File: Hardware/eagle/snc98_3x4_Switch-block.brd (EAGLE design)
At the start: 56.4 x 83.2 mm, 67 parts

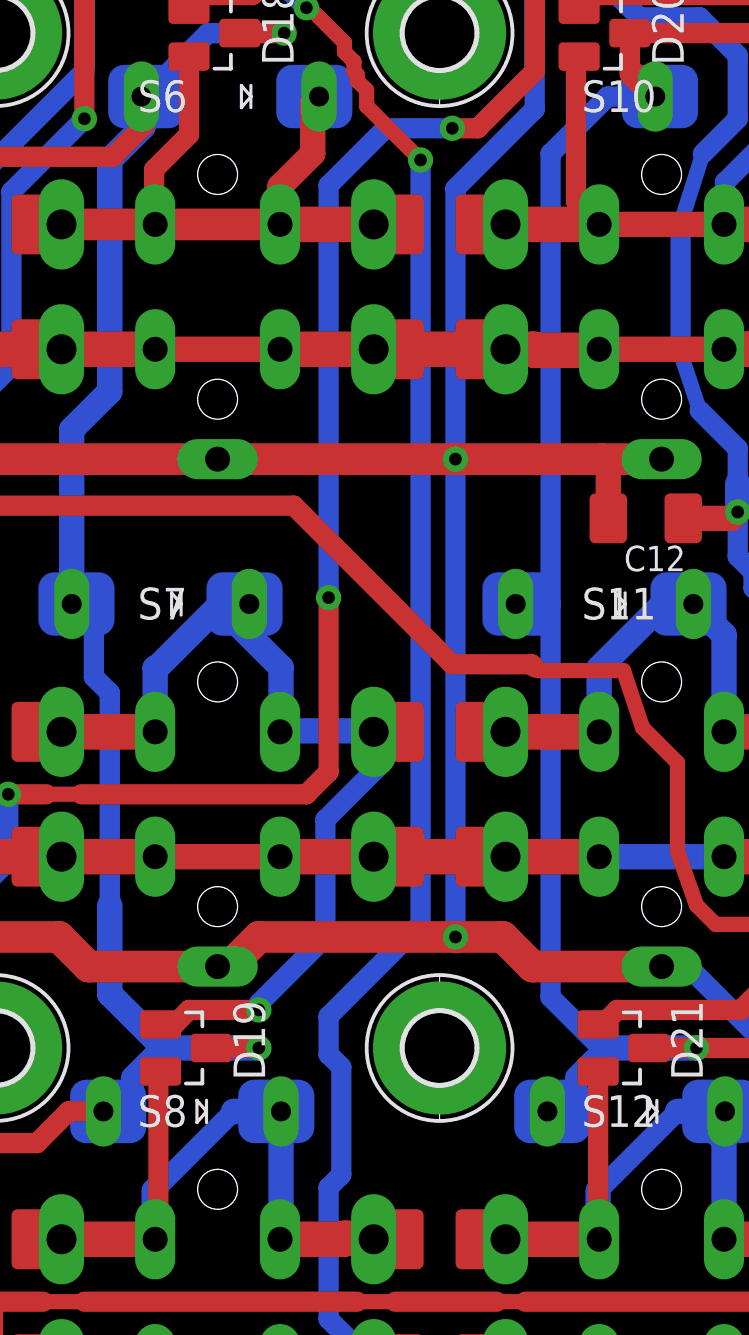
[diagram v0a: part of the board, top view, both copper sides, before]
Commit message: MR(); MS(); M+=(); Display Status
Display whe to or more switch pressed.
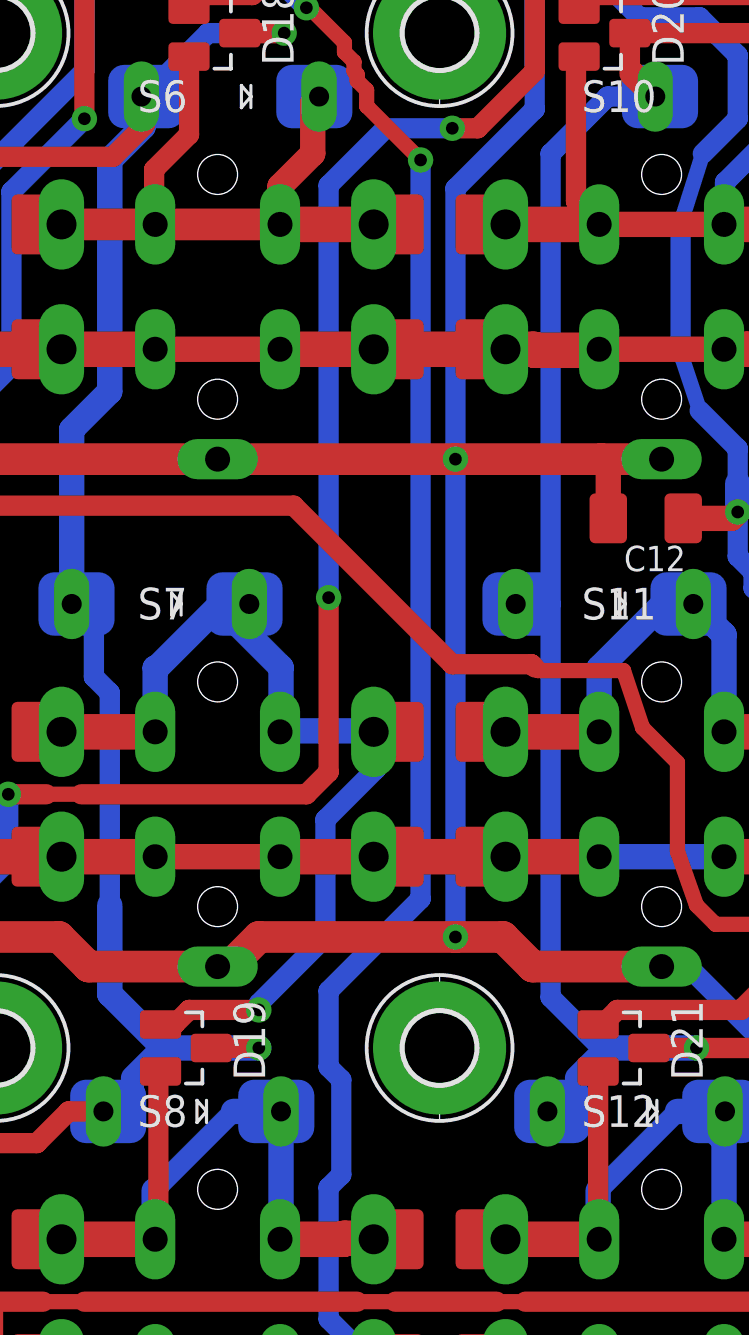
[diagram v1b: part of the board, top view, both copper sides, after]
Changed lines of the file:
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@@
 <setting verticaltext="up"/>
 </settings>
-<grid distance="5" unitdist="mil" unit="mil" style="lines" multiple="1" display="yes" altdistance="0.01" altunitdist="inch" altunit="inch"/>
+<grid distance="0.1" unitdist="inch" unit="inch" style="lines" multiple="1" display="yes" altdistance="0.01" altunitdist="inch" altunit="inch"/>
 <layers>
 <layer number="1" name="Top" color="4" fill="1" visible="yes" active="yes"/>
@@
 <via x="31.75" y="62.865" extent="1-16" drill="0.508"/>
 <via x="36.322" y="56.769" extent="1-16" drill="0.508"/>
-<wire x1="36.322" y1="56.769" x2="36.322" y2="26.162" width="0.8128" layer="16"/>
+<wire x1="36.322" y1="56.769" x2="36.322" y2="27.178" width="0.8128" layer="16"/>
 <wire x1="32.639" y1="10.354" x2="34.444" y2="8.549" width="0.8128" layer="16"/>
 <wire x1="30.861" y1="66.294" x2="32.639" y2="68.072" width="0.8128" layer="16"/>
@@
 <wire x1="31.877" y1="62.865" x2="33.274" y2="61.468" width="0.6096" layer="1"/>
 <wire x1="30.734" y1="63.881" x2="31.75" y2="62.865" width="0.8128" layer="16"/>
-<wire x1="32.639" y1="20.955" x2="32.639" y2="22.479" width="0.8128" layer="16"/>
-<wire x1="36.322" y1="26.162" x2="32.639" y2="22.479" width="0.8128" layer="16"/>
-<wire x1="32.639" y1="20.955" x2="33.147" y2="20.447" width="0.8128" layer="16"/>
-<wire x1="33.147" y1="20.447" x2="33.147" y2="16.129" width="0.8128" layer="16"/>
+<wire x1="32.639" y1="20.447" x2="32.639" y2="23.495" width="0.8128" layer="16"/>
+<wire x1="36.322" y1="27.178" x2="32.639" y2="23.495" width="0.8128" layer="16"/>
+<wire x1="32.639" y1="20.447" x2="33.147" y2="19.939" width="0.8128" layer="16"/>
+<wire x1="33.147" y1="19.939" x2="33.147" y2="16.129" width="0.8128" layer="16"/>
 <wire x1="33.147" y1="16.129" x2="32.639" y2="15.621" width="0.8128" layer="16"/>
 <wire x1="32.639" y1="15.621" x2="32.639" y2="10.354" width="0.8128" layer="16"/>

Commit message: New Hardware Design V0.4
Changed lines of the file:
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@@
 <setting verticaltext="up"/>
 </settings>
-<grid distance="0.1" unitdist="inch" unit="inch" style="lines" multiple="1" display="yes" altdistance="0.01" altunitdist="inch" altunit="inch"/>
+<grid distance="5" unitdist="mil" unit="mil" style="lines" multiple="1" display="yes" altdistance="0.01" altunitdist="inch" altunit="inch"/>
 <layers>
 <layer number="1" name="Top" color="4" fill="1" visible="yes" active="yes"/>
@@
 <layer number="24" name="bOrigins" color="15" fill="1" visible="yes" active="yes"/>
 <layer number="25" name="tNames" color="7" fill="1" visible="yes" active="yes"/>
-<layer number="26" name="bNames" color="7" fill="1" visible="yes" active="yes"/>
+<layer number="26" name="bNames" color="7" fill="1" visible="no" active="yes"/>
 <layer number="27" name="tValues" color="7" fill="1" visible="no" active="yes"/>
 <layer number="28" name="bValues" color="7" fill="1" visible="no" active="yes"/>
@@
 <wire x1="47.625" y1="57.023" x2="46.736" y2="54.229" width="0.6096" layer="16"/>
 <wire x1="46.736" y1="54.229" x2="46.736" y2="49.022" width="0.8128" layer="16"/>
-<wire x1="46.736" y1="49.022" x2="47.498" y2="46.736" width="0.6096" layer="16"/>
-<wire x1="47.498" y1="46.736" x2="49.022" y2="45.212" width="0.8128" layer="16"/>
-<wire x1="49.022" y1="45.212" x2="49.022" y2="43.815" width="0.8128" layer="16"/>
+<wire x1="46.736" y1="49.022" x2="47.625" y2="46.736" width="0.6096" layer="16"/>
+<wire x1="49.022" y1="45.339" x2="49.022" y2="43.815" width="0.8128" layer="16"/>
 <wire x1="49.022" y1="42.672" x2="49.022" y2="40.894" width="0.8128" layer="16"/>
 <wire x1="49.022" y1="40.894" x2="49.657" y2="40.259" width="0.8128" layer="16"/>
@@
 <wire x1="51.308" y1="37.973" x2="52.578" y2="37.973" width="0.8128" layer="16"/>
 <wire x1="52.578" y1="37.973" x2="54.991" y2="35.56" width="0.8128" layer="16"/>
+<wire x1="47.625" y1="46.736" x2="49.022" y2="45.339" width="0.8128" layer="16"/>
 </signal>
 <signal name="N$21">
@@
 <wire x1="16.256" y1="64.516" x2="13.589" y2="67.183" width="0.6096" layer="16"/>
 <wire x1="13.589" y1="67.183" x2="12.065" y2="67.183" width="0.6096" layer="16"/>
-<wire x1="12.065" y1="67.183" x2="11.811" y2="67.437" width="0.6096" layer="16"/>
+<wire x1="12.065" y1="67.183" x2="11.938" y2="67.31" width="0.6096" layer="16"/>
 <via x="11.176" y="81.661" extent="1-16" drill="0.508"/>
 <wire x1="11.811" y1="82.423" x2="12.065" y2="82.677" width="0.6096" layer="1"/>
@@
 <wire x1="46.609" y1="29.083" x2="46.609" y2="32.639" width="0.6096" layer="1"/>
 <wire x1="46.609" y1="32.639" x2="45.212" y2="34.036" width="0.6096" layer="1"/>
-<wire x1="45.212" y1="34.036" x2="44.45" y2="36.322" width="0.6096" layer="1"/>
-<wire x1="44.45" y1="36.322" x2="41.021" y2="36.322" width="0.6096" layer="1"/>
+<wire x1="45.212" y1="34.036" x2="44.323" y2="36.322" width="0.6096" layer="1"/>
+<wire x1="44.323" y1="36.322" x2="41.021" y2="36.322" width="0.6096" layer="1"/>
 <wire x1="41.021" y1="36.322" x2="40.894" y2="36.449" width="0.6096" layer="1"/>
 <wire x1="40.894" y1="36.449" x2="40.767" y2="36.576" width="0.8128" layer="1"/>
@@
 <via x="15.494" y="42.926" extent="1-16" drill="0.508"/>
 <wire x1="15.494" y1="42.926" x2="31.242" y2="42.926" width="0.8128" layer="1"/>
-<wire x1="11.811" y1="67.437" x2="11.176" y2="69.29820625" width="0.6096" layer="16"/>
+<wire x1="11.938" y1="67.31" x2="11.176" y2="69.29820625" width="0.6096" layer="16"/>
 <wire x1="11.811" y1="82.423" x2="11.811" y2="82.296" width="0.8128" layer="1"/>
 <wire x1="11.811" y1="82.296" x2="11.176" y2="81.661" width="0.8128" layer="1"/>
@@
 <wire x1="8.6995" y1="77.1525" x2="8.636" y2="77.089" width="0.8128" layer="1"/>
 <via x="8.636" y="77.089" extent="1-16" drill="0.508"/>
-<wire x1="7.747" y1="66.167" x2="7.747" y2="64.643" width="0.8128" layer="16"/>
+<wire x1="7.747" y1="66.294" x2="7.747" y2="64.643" width="0.8128" layer="16"/>
 <wire x1="7.747" y1="64.643" x2="9.017" y2="63.373" width="0.8128" layer="16"/>
 <wire x1="9.017" y1="63.373" x2="12.192" y2="63.373" width="0.8128" layer="16"/>
 <wire x1="23.8125" y1="18.669" x2="23.622" y2="18.669" width="0.8128" layer="16"/>
 <wire x1="22.5425" y1="38.989" x2="22.352" y2="38.989" width="0.8128" layer="16"/>
-<wire x1="8.4455" y1="79.629" x2="8.4455" y2="77.4065" width="0.8128" layer="1"/>
+<wire x1="8.4455" y1="79.629" x2="8.4455" y2="77.2795" width="0.8128" layer="1"/>
 <wire x1="8.636" y1="77.089" x2="8.636" y2="76.8985" width="0.6096" layer="16"/>
 <wire x1="8.636" y1="76.8985" x2="9.779" y2="74.93" width="0.6096" layer="16"/>
 <wire x1="9.779" y1="74.93" x2="9.779" y2="68.961" width="0.8128" layer="16"/>
-<wire x1="8.509" y1="66.929" x2="7.747" y2="66.167" width="0.8128" layer="16"/>
-<wire x1="8.509" y1="66.929" x2="9.779" y2="68.961" width="0.6096" layer="16"/>
-<wire x1="8.4455" y1="77.4065" x2="8.636" y2="77.089" width="0.8128" layer="1"/>
+<wire x1="8.382" y1="66.929" x2="9.779" y2="68.961" width="0.6096" layer="16"/>
 <wire x1="24.8285" y1="20.0025" x2="24.8285" y2="19.685" width="0.8128" layer="16"/>
 <wire x1="24.8285" y1="19.685" x2="23.8125" y2="18.669" width="0.8128" layer="16"/>
@@
 <wire x1="23.876" y1="26.924" x2="23.876" y2="23.368" width="1.016" layer="16"/>
 <wire x1="23.876" y1="23.368" x2="26.035" y2="21.209" width="1.016" layer="16"/>
+<wire x1="8.636" y1="77.089" x2="8.4455" y2="77.2795" width="0.8128" layer="1"/>
+<wire x1="8.382" y1="66.929" x2="7.747" y2="66.294" width="0.8128" layer="16"/>
 </signal>
 <signal name="A_3">

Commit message: snc98_main_cpu V1.0
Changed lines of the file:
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@@
 <dimension x1="10.414" y1="11.049" x2="10.414" y2="72.009" x3="-9.398" y3="41.529" textsize="1.778" textratio="15" layer="47" visible="yes"/>
 <dimension x1="10.414" y1="11.049" x2="45.974" y2="11.049" x3="28.194" y3="-9.652" textsize="1.778" textratio="15" layer="47" visible="yes"/>
-<dimension x1="0" y1="0" x2="56.388" y2="0" x3="28.194" y3="-18.923" textsize="1.778" textratio="15" layer="47"/>
-<dimension x1="3.302" y1="3.302" x2="53.086" y2="3.302" x3="28.194" y3="-13.97" textsize="1.778" textratio="15" layer="47"/>
-<dimension x1="53.086" y1="3.302" x2="53.086" y2="41.529" x3="60.96" y3="22.4155" textsize="1.778" textratio="15" layer="47"/>
-<dimension x1="53.086" y1="3.302" x2="53.086" y2="79.756" x3="66.294" y3="41.529" textsize="1.778" textratio="15" layer="47"/>
+<dimension x1="0" y1="0" x2="56.388" y2="0" x3="28.194" y3="-18.923" textsize="1.778" textratio="15" layer="47" visible="yes"/>
+<dimension x1="3.302" y1="3.302" x2="53.086" y2="3.302" x3="28.194" y3="-13.97" textsize="1.778" textratio="15" layer="47" visible="yes"/>
+<dimension x1="53.086" y1="3.302" x2="53.086" y2="41.529" x3="60.96" y3="22.4155" textsize="1.778" textratio="15" layer="47" visible="yes"/>
+<dimension x1="53.086" y1="3.302" x2="53.086" y2="79.756" x3="66.294" y3="41.529" textsize="1.778" textratio="15" layer="47" visible="yes"/>
 <wire x1="3.048" y1="83.185" x2="0" y2="80.137" width="0" layer="20" curve="90"/>
 <wire x1="56.388" y1="80.137" x2="53.34" y2="83.185" width="0" layer="20" curve="90"/>
 <wire x1="0" y1="3.048" x2="3.048" y2="0" width="0" layer="20" curve="90"/>
 <wire x1="53.34" y1="0" x2="56.388" y2="3.048" width="0" layer="20" curve="90"/>
+<dimension x1="10.414" y1="72.009" x2="10.414" y2="80.264" x3="-9.398" y3="76.1365" textsize="1.778" textratio="15" layer="47" visible="yes"/>
 </plain>
 <attributes>
@@
 <wire x1="31.877" y1="62.865" x2="33.274" y2="61.468" width="0.6096" layer="1"/>
 <wire x1="30.734" y1="63.881" x2="31.75" y2="62.865" width="0.8128" layer="16"/>
-<wire x1="32.639" y1="20.447" x2="32.639" y2="23.495" width="0.8128" layer="16"/>
-<wire x1="36.322" y1="27.178" x2="32.639" y2="23.495" width="0.8128" layer="16"/>
-<wire x1="32.639" y1="20.447" x2="33.147" y2="19.939" width="0.8128" layer="16"/>
-<wire x1="33.147" y1="19.939" x2="33.147" y2="16.129" width="0.8128" layer="16"/>
+<wire x1="33.147" y1="24.003" x2="33.147" y2="16.129" width="0.8128" layer="16"/>
 <wire x1="33.147" y1="16.129" x2="32.639" y2="15.621" width="0.8128" layer="16"/>
 <wire x1="32.639" y1="15.621" x2="32.639" y2="10.354" width="0.8128" layer="16"/>
@@
 <wire x1="12.914" y1="8.549" x2="16.664" y2="8.549" width="1.016" layer="1"/>
 <wire x1="21.944" y1="8.549" x2="25.694" y2="8.549" width="1.016" layer="1"/>
+<wire x1="36.322" y1="27.178" x2="33.147" y2="24.003" width="0.8128" layer="16"/>
 </signal>
 <signal name="C3">
@@
 <wire x1="32.258" y1="77.724" x2="34.798" y2="77.724" width="1.016" layer="1"/>
 <wire x1="34.798" y1="77.724" x2="34.925" y2="77.597" width="1.016" layer="1"/>
-<wire x1="34.925" y1="77.597" x2="35.56" y2="77.597" width="0.8128" layer="1"/>
-<wire x1="35.56" y1="77.597" x2="36.195" y2="76.962" width="0.8128" layer="1"/>
-<wire x1="36.195" y1="76.962" x2="36.576" y2="76.962" width="0.8128" layer="1"/>
-<wire x1="36.576" y1="76.962" x2="36.957" y2="76.581" width="0.8128" layer="1"/>
-<wire x1="36.957" y1="76.581" x2="36.957" y2="76.454" width="0.8128" layer="1"/>
-<wire x1="36.957" y1="76.454" x2="37.084" y2="76.327" width="0.8128" layer="1"/>
+<wire x1="34.925" y1="77.597" x2="35.814" y2="77.597" width="0.8128" layer="1"/>
+<wire x1="35.814" y1="77.597" x2="36.957" y2="76.454" width="0.8128" layer="1"/>
 <wire x1="37.084" y1="76.327" x2="37.084" y2="72.898" width="0.6096" layer="1"/>
 <wire x1="37.084" y1="72.898" x2="36.195" y2="72.009" width="0.6096" layer="1"/>
@@
 <wire x1="5.588" y1="64.262" x2="4.191" y2="62.865" width="0.8128" layer="1"/>
 <wire x1="4.191" y1="62.865" x2="1.651" y2="62.865" width="0.8128" layer="1"/>
+<wire x1="36.957" y1="76.454" x2="37.084" y2="76.454" width="0.254" layer="1"/>
+<wire x1="37.084" y1="76.454" x2="37.084" y2="76.327" width="0.254" layer="1"/>
 </signal>
 <signal name="GND">
@@
 <wire x1="12.065" y1="67.183" x2="11.938" y2="67.31" width="0.6096" layer="16"/>
 <via x="11.176" y="81.661" extent="1-16" drill="0.508"/>
-<wire x1="11.811" y1="82.423" x2="12.065" y2="82.677" width="0.6096" layer="1"/>
 <wire x1="38.481" y1="81.407" x2="38.481" y2="80.518" width="0.8128" layer="1"/>
 <wire x1="38.481" y1="80.518" x2="38.354" y2="80.391" width="0.8128" layer="1"/>
 <wire x1="11.176" y1="69.342" x2="11.176" y2="69.29820625" width="0.6096" layer="16"/>
-<wire x1="37.211" y1="82.677" x2="38.481" y2="81.407" width="0.6096" layer="1"/>
-<wire x1="37.211" y1="82.677" x2="12.065" y2="82.677" width="0.6096" layer="1"/>
+<wire x1="37.211" y1="82.677" x2="12.319" y2="82.677" width="0.6096" layer="1"/>
 <wire x1="11.176" y1="81.661" x2="11.176" y2="77.978" width="0.8128" layer="16"/>
 <wire x1="11.176" y1="77.978" x2="11.811" y2="77.343" width="0.8128" layer="16"/>
@@
 <wire x1="15.494" y1="42.926" x2="31.242" y2="42.926" width="0.8128" layer="1"/>
 <wire x1="11.938" y1="67.31" x2="11.176" y2="69.29820625" width="0.6096" layer="16"/>
-<wire x1="11.811" y1="82.423" x2="11.811" y2="82.296" width="0.8128" layer="1"/>
-<wire x1="11.811" y1="82.296" x2="11.176" y2="81.661" width="0.8128" layer="1"/>
+<wire x1="12.065" y1="82.55" x2="11.176" y2="81.661" width="0.8128" layer="1"/>
+<wire x1="12.192" y1="82.55" x2="11.938" y2="82.296" width="0.6096" layer="1"/>
+<wire x1="38.481" y1="81.407" x2="37.338" y2="82.55" width="0.8128" layer="1"/>
+<wire x1="37.338" y1="82.55" x2="37.211" y2="82.677" width="0.6096" layer="1"/>
+<wire x1="12.319" y1="82.677" x2="12.192" y2="82.55" width="0.6096" layer="1"/>
+<wire x1="12.192" y1="82.55" x2="12.065" y2="82.55" width="0.6096" layer="1"/>
 </signal>
 <signal name="A_1">

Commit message: V 5.0 Hardware - Design
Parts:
- moved C11 21.6 mm to (37.1, 16.8), turned to 180 degrees
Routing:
- net GND: track 259.3 -> 268.9 mm
- net A2: track 146.9 -> 149.2 mm
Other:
- outline, holes or cut-outs redrawn

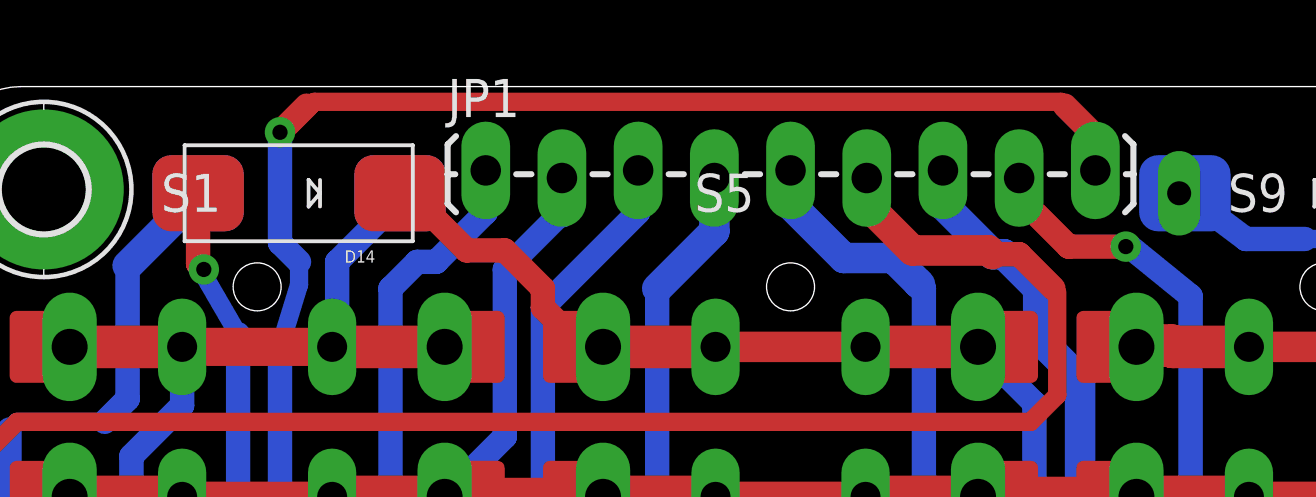
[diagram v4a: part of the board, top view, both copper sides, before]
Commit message: PCB cleaning V1.1
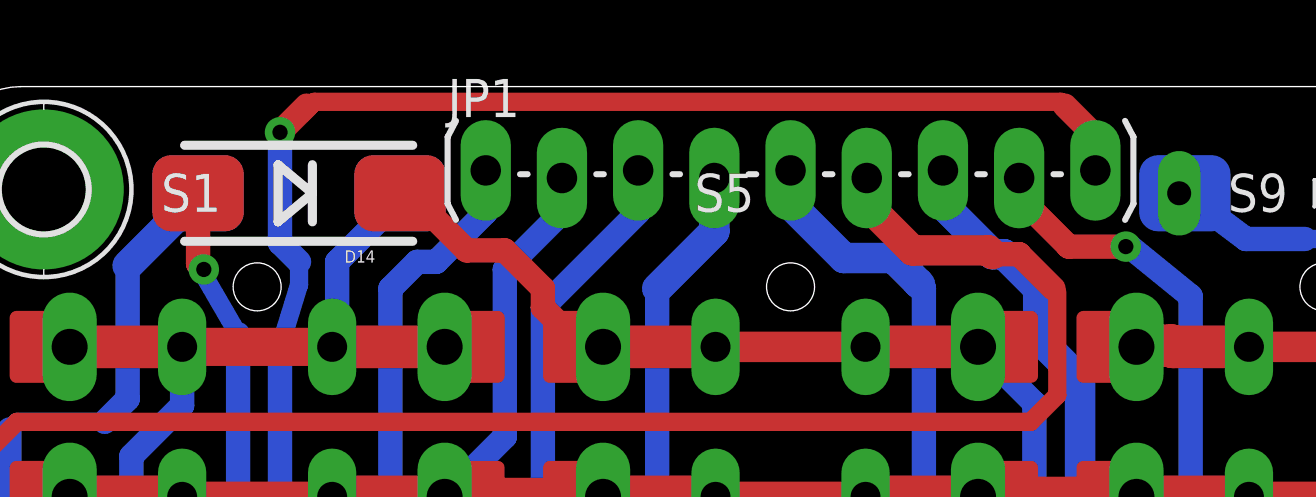
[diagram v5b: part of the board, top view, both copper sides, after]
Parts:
- JP1: value (none) -> M09LOCK-LONGPADS
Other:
- board text added: "snc98 3x4 Switch-block Rev. 0.4"
- board text removed: "snc98 3x4 Switch-block Rev. 0.3"

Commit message: sinh()_cosh()_tanh() added
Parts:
- H10, H2, H3, H9: value MOUNT-PAD-ROUND2.8 -> MOUNT-PAD-ROUND2.3; device holes:2,8-PAD -> holes:2,3-PAD
